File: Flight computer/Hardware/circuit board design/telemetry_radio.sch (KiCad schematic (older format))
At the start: 23 parts, among them U10 CG2179M2, U3 Si4463, X1 TM-32.000-AF3-33-S

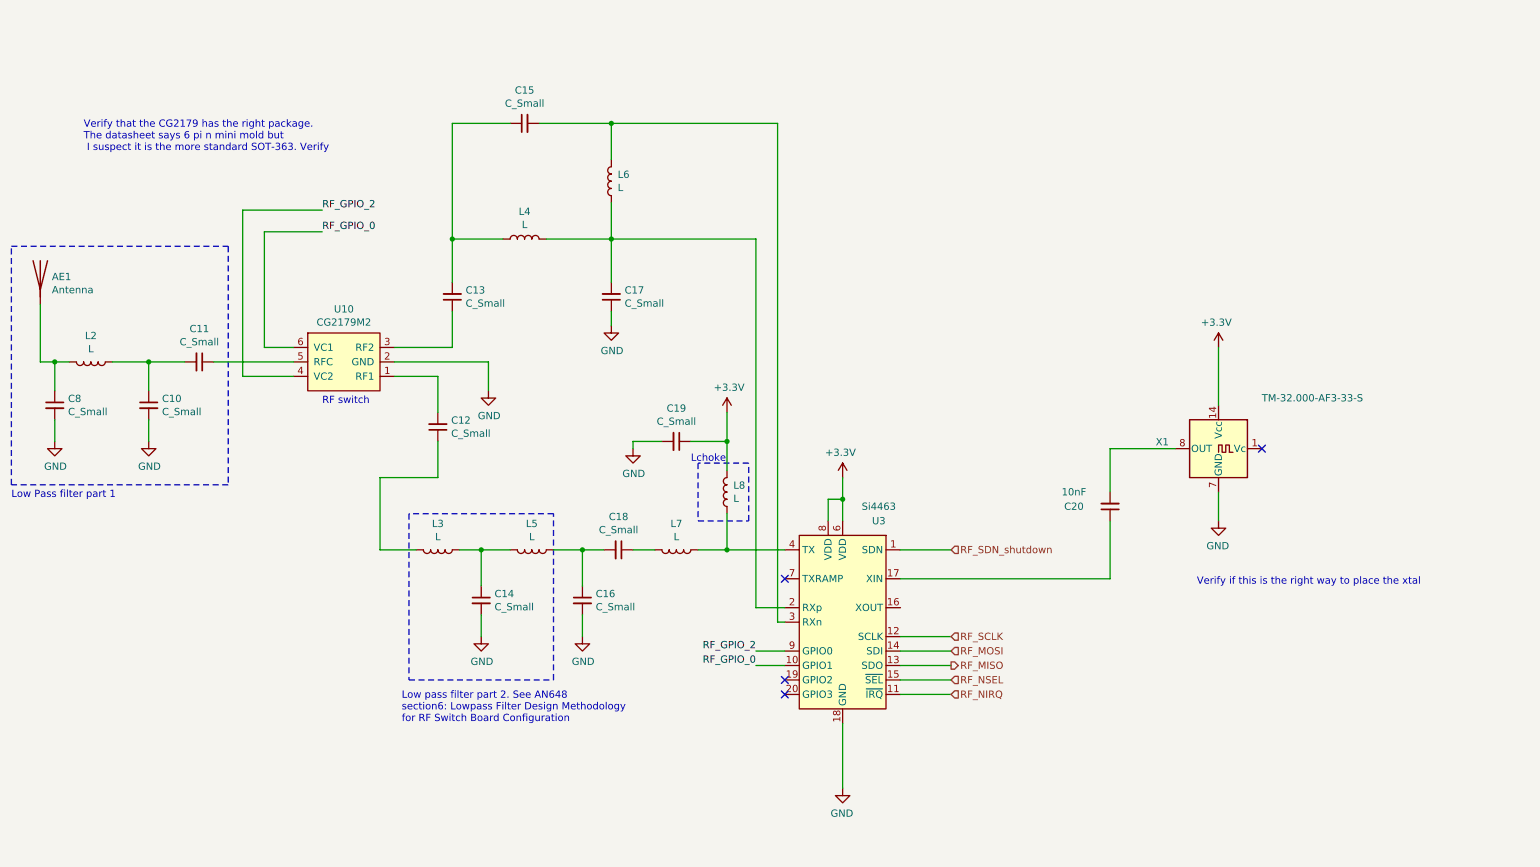
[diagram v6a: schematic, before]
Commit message: worked on the silabs 4463 radio chip
- filled in the component values for TX matching and tx filtering
- filled in tentative values for RX LNA matching. Will have to verify
- swapped out XTAL and put in an RS Pro TCXO. Decoupled its powersupply.
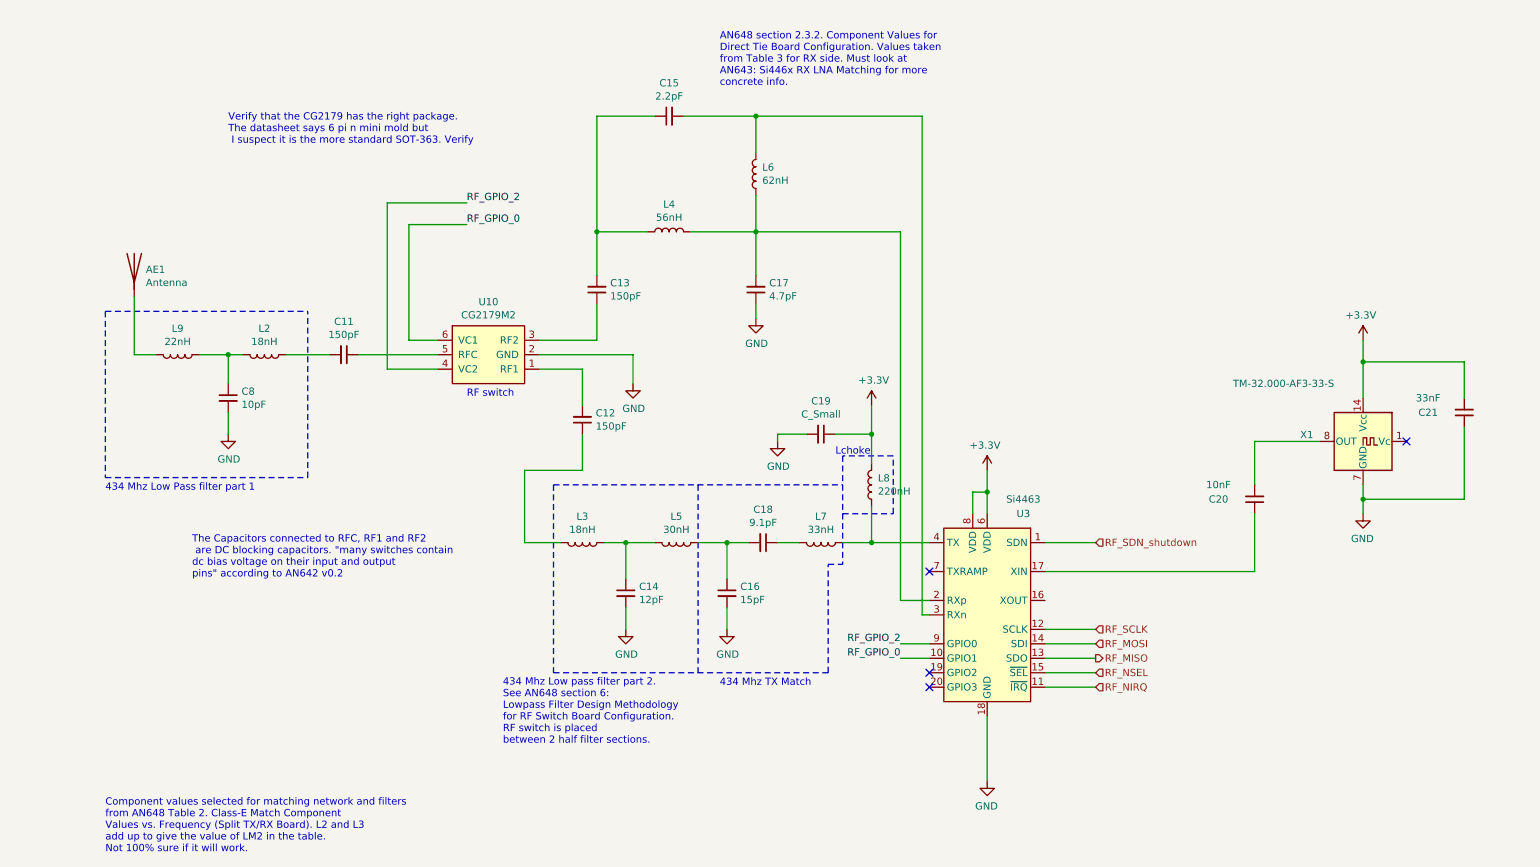
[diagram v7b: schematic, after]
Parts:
- removed C10: C_Small, symbol Device:C_Small
- added C21: 33nF, symbol Device:C_Small
- added L9: 22nH, symbol Device:L
- C11, C12, C13: value C_Small -> 150pF
- C14: value C_Small -> 12pF
- C15: value C_Small -> 2.2pF
- C16: value C_Small -> 15pF
- C17: value C_Small -> 4.7pF
- C18: value C_Small -> 9.1pF
- C8: value C_Small -> 10pF
- L2, L3: value L -> 18nH
- L4: value L -> 56nH
- L5: value L -> 30nH
- L6: value L -> 62nH
- L7: value L -> 33nH
- L8: value L -> 220nH
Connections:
- net +3V3: now also C21.2
- net GND: now also C21.1
- net at C8.1, L2.2: now also L9.1; no longer AE1.1 (A)
- new net: AE1.1 (A), L9.2
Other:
- note added: "434 Mhz Low Pass filter part 1\n"
- note added: "434 Mhz Low pass filter part 2. \nSee AN648 section 6:\nLowpass Filter Design Methodology \nfor RF Switch Board Configuration. \nRF switch is placed \nbetween 2 half filter sections."
- note added: "434 Mhz TX Match"
- note added: "AN648 section 2.3.2. Component Values for\nDirect Tie Board Configuration. Values taken \nfrom Table 3 for RX side. Must look at\nAN643: Si446x RX LNA Matching for more\nconcrete info."
- note added: "Component values selected for matching network and filters \nfrom AN648 Table 2. Class-E Match Component \nValues vs. Frequency (Split TX/RX Board). L2 and L3 \nadd up to give the value of LM2 in the table. \nNot 100% sure if it will work."
- note added: "The Capacitors connected to RFC, RF1 and RF2\n are DC blocking capacitors. "many switches contain \ndc bias voltage on their input and output \npins" according to AN642 v0.2"
- note removed: "Low Pass filter part 1\n"
- note removed: "Low pass filter part 2. See AN648\nsection6: Lowpass Filter Design Methodology \nfor RF Switch Board Configuration"
- note removed: "Verify if this is the right way to place the xtal"
- moved on the sheet: AE1, C11, C12, C13, C14, C15, C16, C17, C18, C19, C20, C8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

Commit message: Work in progress for Telemetry Radio
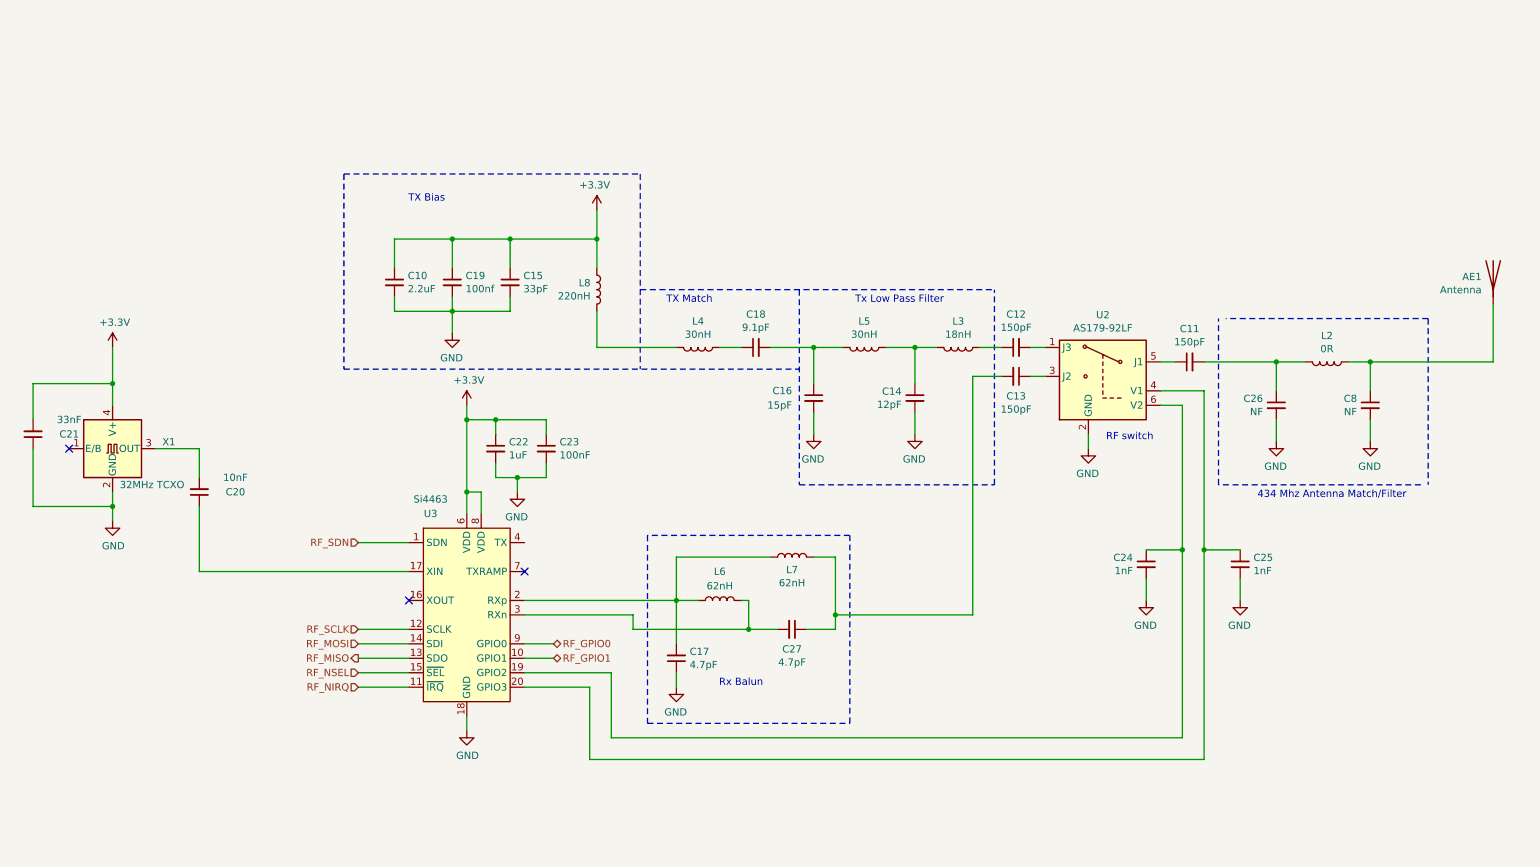
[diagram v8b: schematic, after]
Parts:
- removed L9: 22nH, symbol Device:L
- removed U10: CG2179M2, Package_TO_SOT_SMD:SOT-363_SC-70-6_Handsoldering, symbol RF_Switch:CG2179M2
- removed X1: TM-32.000-AF3-33-S, symbol Oscillator:TM-32.000-AF3-33-S
- added C10: 2.2uF, symbol Device:C_Small
- added C22: 1uF, symbol Device:C_Small
- added C23: 100nF, symbol Device:C_Small
- added C24, C25: 1nF, symbol Device:C_Small
- added C26: NF, symbol Device:C_Small
- added C27: 4.7pF, symbol Device:C_Small
- added U2: AS179-92LF, Package_TO_SOT_SMD:SOT-363_SC-70-6, symbol RF_Switch:AS179-92LF
- added X1: 32MHz TCXO, Oscillator:Oscillator_SMD_IQD_IQXO70-4Pin_7.5x5.0mm, symbol Oscillator:IQXO-70
- C15: value 2.2pF -> 33pF
- C19: value C_Small -> 100nf
- C8: value 10pF -> NF
- L2: value 18nH -> 0R
- L4: value 56nH -> 30nH
- L7: value 33nH -> 62nH
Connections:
- net +3V3: now also C15.1, C10.1, C22.1, C23.1, X1.4 (V+)
- net GND: now also C15.2, C10.2, C22.2, C23.2, C24.2, C25.2, C26.2, U2.2 (GND), X1.2 (GND)
- net at U3.19 (GPIO2): now also C24.1, U2.6 (V2)
- net at C17.2, U3.2 (RXp): now also L6.2, L7.2; no longer L4.2, L6.1
- net at U3.20 (GPIO3): now also C25.1, U2.4 (V1)
- net at C12.2: now also U2.1 (J3)
- net at C13.1: now also U2.3 (J2)
- net at C11.1: now also U2.5 (J1)
- net at C20.2: now also X1.3 (OUT)
- net at AE1.1 (A): now also C8.1, L2.2
- net at C11.2, L2.1: now also C26.1
- net at C18.1: now also L4.2; no longer L7.2
- net RF_GPIO_0 renamed RF_GPIO1
- net RF_GPIO_2 renamed RF_GPIO0
- net RF_SDN_shutdown renamed RF_SDN
- new net: C27.2, L6.1, U3.3 (RXn)
- new net: L4.1, L8.1
- new net: C13.2, C27.1, L7.1
- now unconnected: U3.4 (TX)
- no-connect marks 4 -> 3
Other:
- note added: "434 Mhz Antenna Match/Filter"
- note added: "Rx Balun"
- note added: "TX Bias"
- note added: "TX Match"
- note added: "Tx Low Pass Filter"
- note removed: "434 Mhz Low Pass filter part 1\n"
- note removed: "434 Mhz Low pass filter part 2. \nSee AN648 section 6:\nLowpass Filter Design Methodology \nfor RF Switch Board Configuration. \nRF switch is placed \nbetween 2 half filter sections."
- note removed: "434 Mhz TX Match"
- note removed: "AN648 section 2.3.2. Component Values for\nDirect Tie Board Configuration. Values taken \nfrom Table 3 for RX side. Must look at\nAN643: Si446x RX LNA Matching for more\nconcrete info."
- note removed: "Component values selected for matching network and filters \nfrom AN648 Table 2. Class-E Match Component \nValues vs. Frequency (Split TX/RX Board). L2 and L3 \nadd up to give the value of LM2 in the table. \nNot 100% sure if it will work."
- note removed: "Lchoke\n"
- note removed: "The Capacitors connected to RFC, RF1 and RF2\n are DC blocking capacitors. "many switches contain \ndc bias voltage on their input and output \npins" according to AN642 v0.2"
- note removed: "Verify that the CG2179 has the right package. \nThe datasheet says 6 pi n mini mold but\n I suspect it is the more standard SOT-363. Verify"
- moved on the sheet: AE1, C11, C12, C13, C14, C16, C17, C18, C19, C20, C21, C8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
